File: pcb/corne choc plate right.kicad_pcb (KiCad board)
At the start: 2 copper layers, 136.2 x 88.4 mm, 27 parts, among them SW1 SW_PUSH, SW10 SW_PUSH, SW11 SW_PUSH, SW12 SW_PUSH, SW13 SW_PUSH, SW14 SW_PUSH, SW15 SW_PUSH, SW16 SW_PUSH, SW17 SW_PUSH, SW18 SW_PUSH, SW19 SW_PUSH, SW2 SW_PUSH, SW20 SW_PUSH, SW3 SW_PUSH, SW4 SW_PUSH, SW45 SW_PUSH, SW46 SW_PUSH, SW5 SW_PUSH, SW6 SW_PUSH, SW7 SW_PUSH, SW8 SW_PUSH, SW9 SW_PUSH

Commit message: v2.1: thumb arc, key-following edges, roomier trackpoint
- Thumb keys on one arc on both halves (0/15/30 degrees); the split inner
  keys turn like the others and stack one row apart (tools/thumbs.py).
- Edge round the thumbs redrawn from the keys: 0.95 mm from the inner
  keycaps, one level line under the middle and outer keys, and a 60-degree
  outer slant cornered off the trackpoint sensor. Halves identical.
- Trackpoint stem 3.4 mm lower in the same board footprint.
- Holykeebs and Corne logos removed.
- Separate right switch plate with an opening for the sensor.
- Router stops on the copper it is joining; ground islands are joined to
  the main ground; sensor links routed like other nets.
- Renders use KLP Lame keycaps; tools/demo.sh rebuilds them.
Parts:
- removed SW19: SW_PUSH, kbd:SW_Hole
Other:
- outline, holes or cut-outs redrawn
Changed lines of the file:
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@@
-	(footprint "kbd:SW_Hole"
-		(layer "F.Cu")
-		(at 202.7125 117.52 180)
-		(property "Reference" "SW19"
-			(at 7 8.1 180)
-			(layer "F.SilkS")
-			(hide yes)
-			(effects
-				(font
-					(size 1 1)
-					(thickness 0.15)
-				)
-			)
-		)
-		(property "Value" "SW_PUSH"
-			(at -7.4 -8.1 180)
-			(layer "F.Fab")
-			(hide yes)
-			(effects
-				(font
-					(size 1 1)
-					(thickness 0.15)
-				)
-			)
-		)
-		(property "Datasheet" ""
-			(at 0 0 180)
-			(layer "F.Fab")
-			(hide yes)
-			(effects
-				(font
-					(size 1.27 1.27)
-				)
-			)
-		)
-		(property "Description" ""
-			(at 0 0 180)
-			(layer "F.Fab")
-			(hide yes)
-			(effects
-				(font
-					(size 1.27 1.27)
-				)
-			)
-		)
-		(attr through_hole)
-		(duplicate_pad_numbers_are_jumpers no)
-		(fp_line
-			(start 7 7)
-			(end 7 -7)
-			(stroke
-				(width 0.12)
-				(type solid)
-			)
-			(layer "Edge.Cuts")
-		)
-		(fp_line
-			(start 7 -7)
-			(end -7 -7)
-			(stroke
-				(width 0.12)
-				(type solid)
-			)
-			(layer "Edge.Cuts")
-		)
-		(fp_line
-			(start -7 7)
-			(end 7 7)
-			(stroke
-				(width 0.12)
-				(type solid)
-			)
-			(layer "Edge.Cuts")
-		)
-		(fp_line
-			(start -7 -7)
-			(end -7 7)
-			(stroke
-				(width 0.12)
-				(type solid)
-			)
-			(layer "Edge.Cuts")
-		)
-		(fp_line
-			(start 9.525 9.525)
-			(end 9.525 -9.525)
-			(stroke
-				(width 0.15)
-				(type solid)
-			)
-			(layer "F.Fab")
-		)
-		(fp_line
-			(start 9.525 -9.525)
-			(end -9.525 -9.525)
-			(stroke
-				(width 0.15)
-				(type solid)
-			)
-			(layer "F.Fab")
-		)
-		(fp_line
-			(start -9.525 9.525)
-			(end 9.525 9.525)
-			(stroke
-				(width 0.15)
-				(type solid)
-			)
-			(layer "F.Fab")
-		)
-		(fp_line
-			(start -9.525 -9.525)
-			(end -9.525 9.525)
-			(stroke
-				(width 0.15)
-				(type solid)
-			)
-			(layer "F.Fab")
-		)
-		(embedded_fonts no)
-	)
 	(footprint "kbd:SW_Hole"
 		(layer "F.Cu")
@@
 	)
 	(gr_poly
+		(pts
+			(xy 209.510001 109.760192) (xy 209.619809 109.87) (xy 209.660001 110.02) (xy 209.660001 128.41) (xy 209.619809 128.56)
+			(xy 209.510001 128.669808) (xy 209.360001 128.71) (xy 196.060001 128.71) (xy 195.910001 128.669808)
+			(xy 195.800193 128.56) (xy 195.760001 128.41) (xy 195.760001 110.02) (xy 195.800193 109.87) (xy 195.910001 109.760192)
+			(xy 196.060001 109.72) (xy 209.360001 109.72)
+		)
+		(stroke
+			(width 0.05)
+			(type default)
+		)
+		(fill no)
+		(layer "Edge.Cuts")
+	)
+	(gr_poly

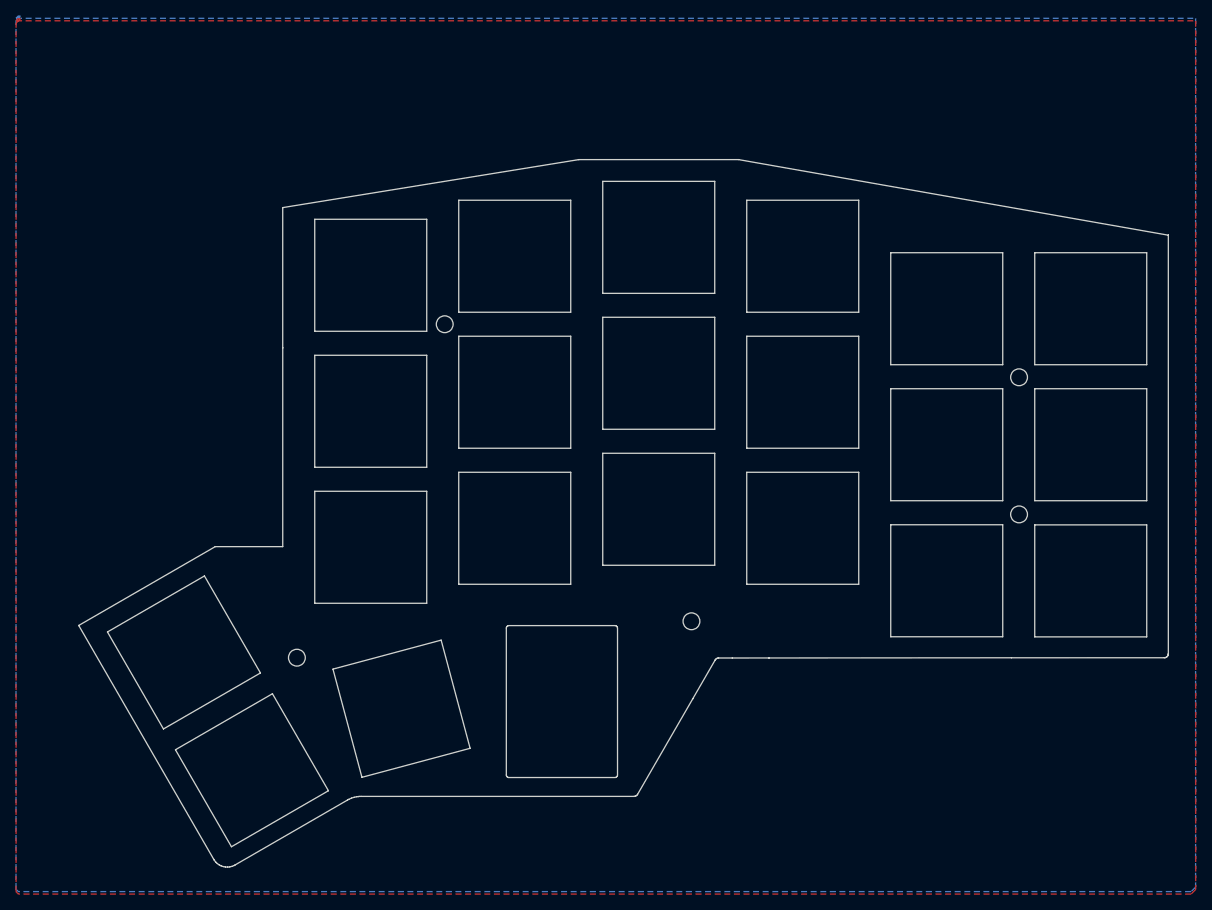
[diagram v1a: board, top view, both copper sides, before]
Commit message: v2.1: 1.15 mm key-to-edge gap, matching switch orientation, LED moves
- Keycaps sit 1.15 mm from the edge wherever it follows them; outer side
  edges move out, and every hot-swap socket pad clears the edge by 0.33 mm.
- The left inner thumb keys no longer turn 180 degrees: every switch, and
  every per-key LED, faces the same way.
- Underglow LED32 and its left twin LED5 move, mirrored, clear of the
  trackpoint driver's hand-soldered pads.
- Mounting holes for the unused OLED cover removed (tools/strip.py).
- Plates follow the moved outer edges; renders show both plates fitted.
- Build: finish pass runs until no dangling copper is left.
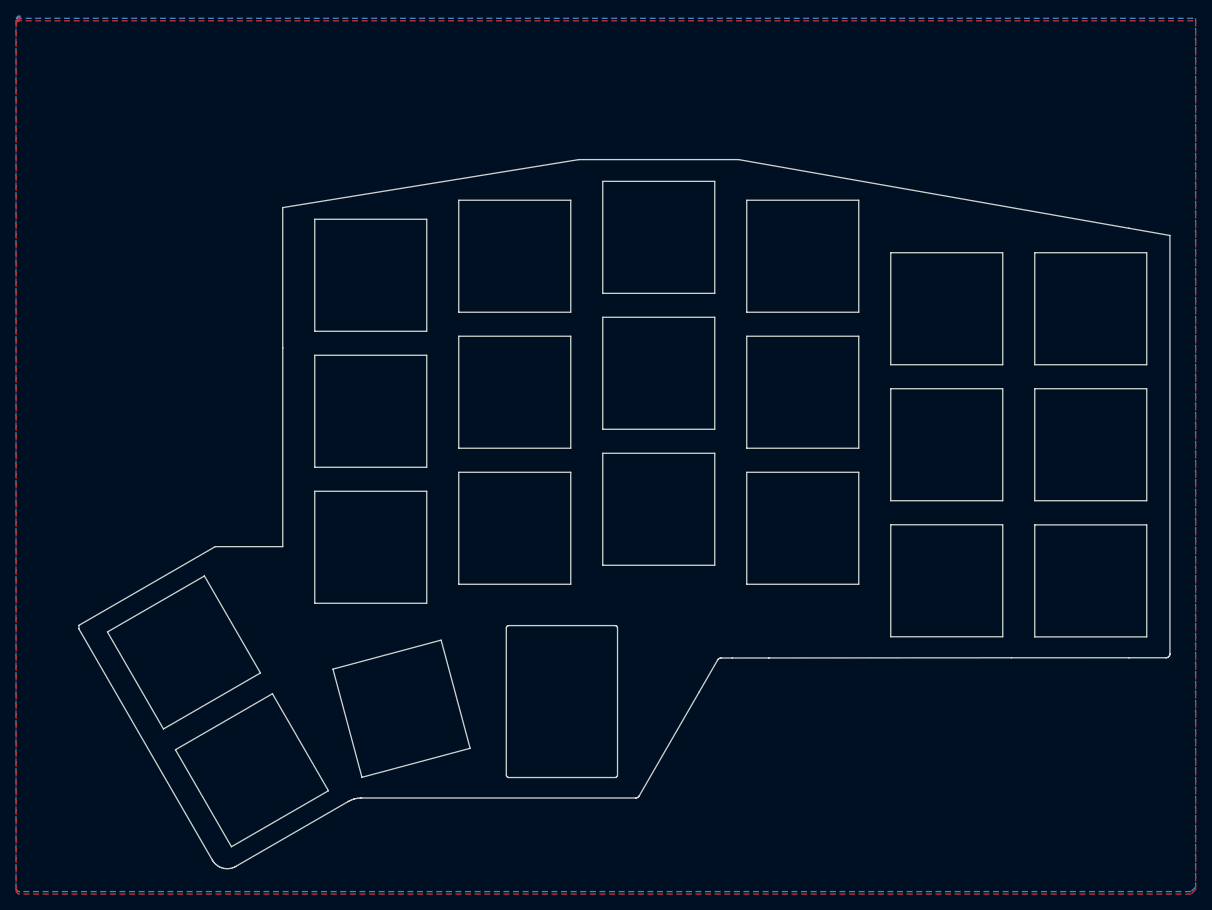
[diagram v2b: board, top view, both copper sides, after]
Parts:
- removed ?: M2_HOLE_NPH, holykeebs:M2_HOLE_NPH
- removed h2 (x4): h2, holykeebs:M2_HOLE_NPH
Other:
- board size 136.2 x 88.4 mm -> 136.4 x 88.6 mm

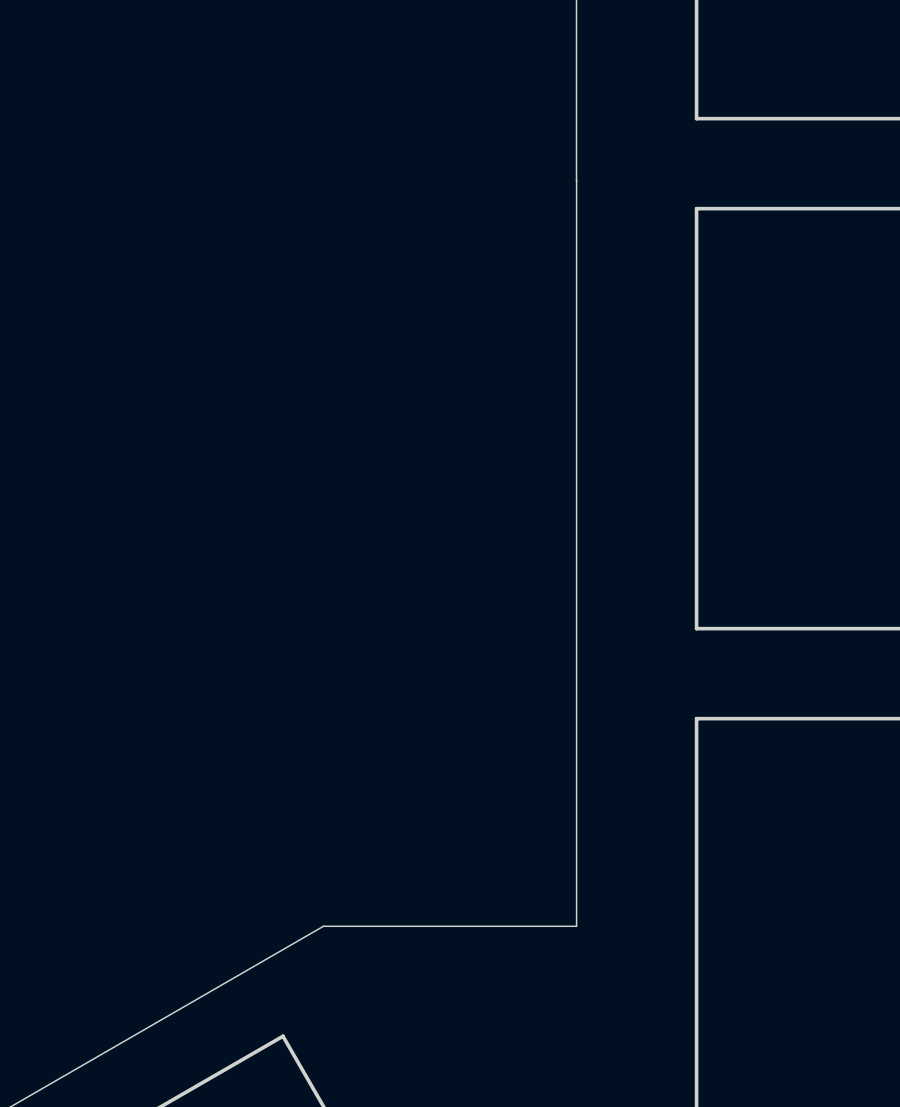
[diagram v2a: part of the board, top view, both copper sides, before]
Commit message: v2.1: driver pads per drawing, diagonal plate edge, no-OLED renders
- Trackpoint driver host pads follow Sprintek's drawing: 1.0 mm wide at
  1.80 mm pitch, leaving 0.8 mm between them for hand soldering.
- The switch plate carries the upper inner thumb key's top edge straight
  on to its inner edge (2.6 mm clear of the OLED header) instead of a step.
- Render script gains assembled top-down and no-OLED views.
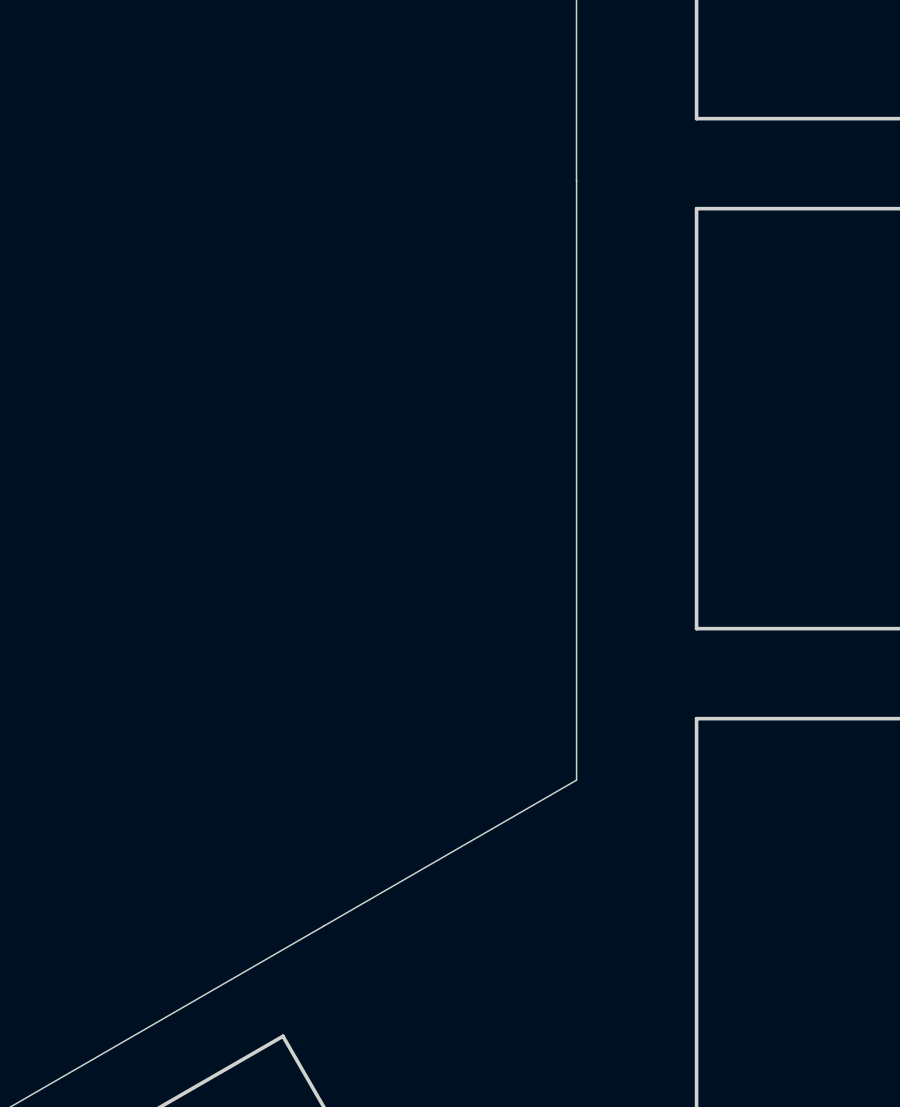
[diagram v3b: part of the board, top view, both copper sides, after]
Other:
- outline, holes or cut-outs redrawn
